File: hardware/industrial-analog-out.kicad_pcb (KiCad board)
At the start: 2 copper layers, 40 x 40 mm, 52 parts, among them P1 CON-SENSOR2, P2 CONN_8, P3 DEBUG, P4 BOOT, U1 LMR62014X, U2 XMC1XXX24, U3 DACX760, U4 DRILL, U5 DRILL, U6 DRILL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

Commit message: Add all logos
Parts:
- added G***: LOGO, kicad-libraries:Logo_CoMCU, B.Cu at (124.6, 116.3)
- VAL: footprint kicad-libraries:WEEE_7mm_back -> kicad-libraries:WEEE_7mm
- moved VAL 32.2 mm to (146.6, 116.3)
- moved VAL 18.7 mm to (135.6, 116.3), turned to 270 degrees

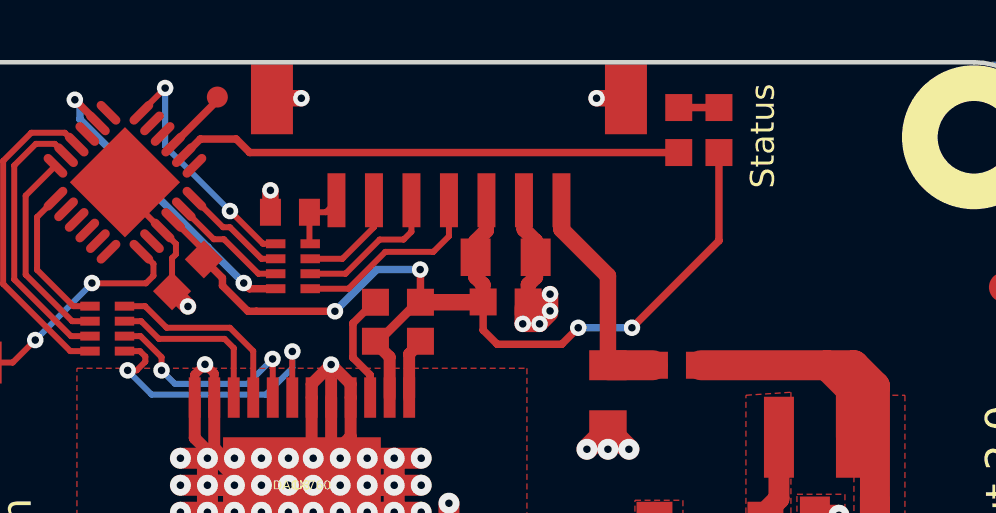
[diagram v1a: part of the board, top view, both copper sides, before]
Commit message: added second led, not fully routed
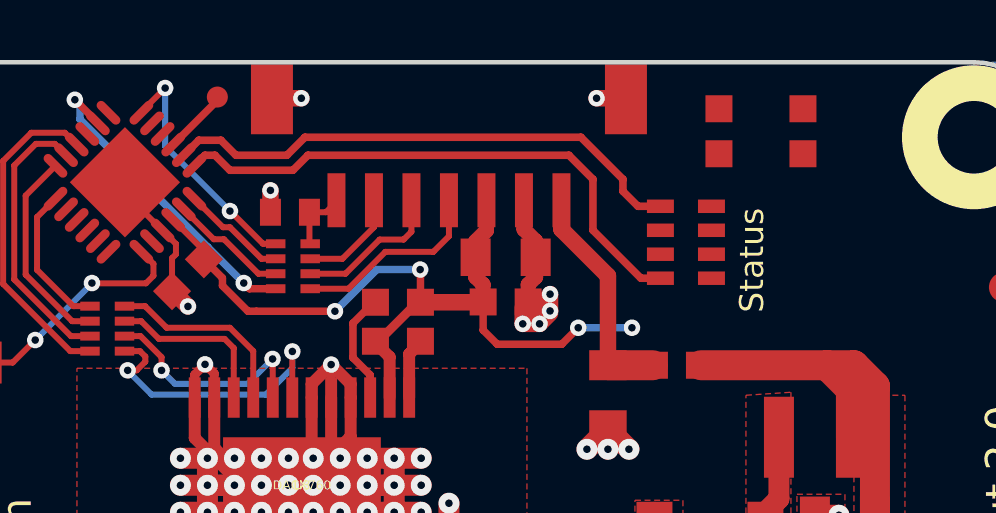
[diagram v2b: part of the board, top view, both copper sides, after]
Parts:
- removed R9: 1k, kicad-libraries:R0603F
- added D6: LED, kicad-libraries:D0603F, F.Cu at (147.4, 82.3)
- added RP3: 1k, kicad-libraries:4X0603, F.Cu at (143.5, 86.0)
- turned D5 to 270 degrees
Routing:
- net Net-(RP3-Pad5): track 0.00 -> 18.8 mm
- net 3V3: track 35.0 -> 28.0 mm
- net Net-(D5-Pad2): track 1.34 -> 0.00 mm
- net Net-(RP3-Pad8): track 16.9 -> 17.7 mm

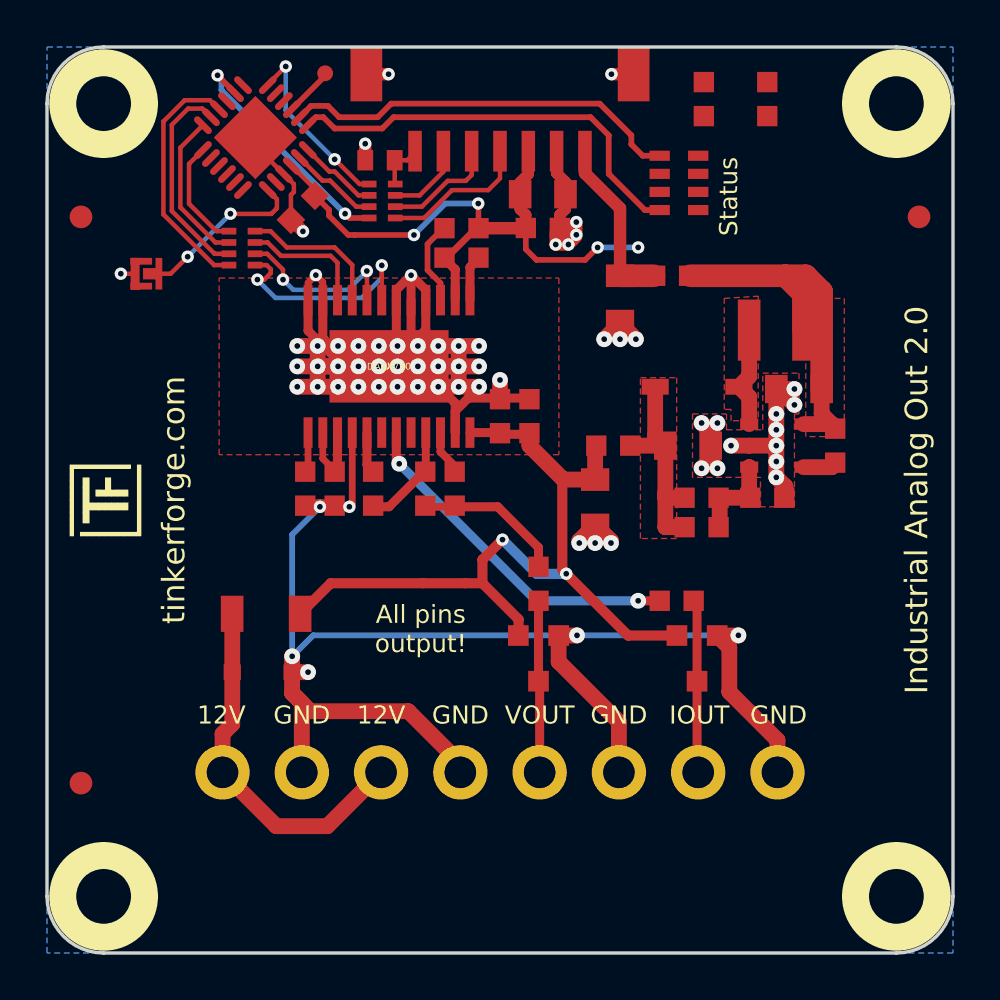
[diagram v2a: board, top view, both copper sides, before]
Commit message: routing finished, logo placement fixed
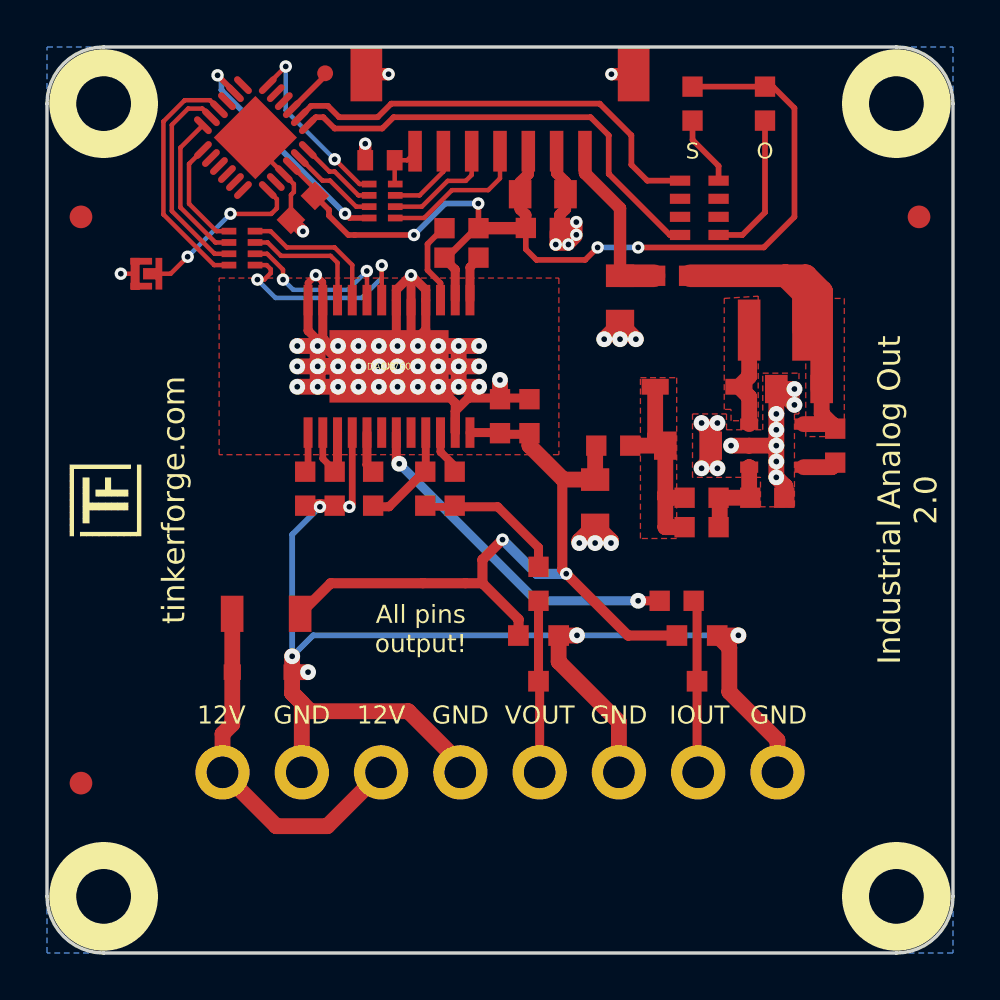
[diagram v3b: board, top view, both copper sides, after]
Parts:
- moved G*** 26.6 mm to (145.6, 100.0), turned to 90 degrees
- moved VAL 26.6 mm to (125.6, 100.0), turned to 90 degrees
- moved VAL 16.3 mm to (135.6, 100.0), turned to 90 degrees
- moved RP3 1.42 mm to (144.4, 87.1)
- moved D5 0.54 mm to (144.1, 82.5)
- moved D6 0.22 mm to (147.3, 82.5)
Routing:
- net 3V3: track 28.0 -> 45.2 mm
- net Net-(D6-Pad2): track 0.00 -> 6.51 mm
- net Net-(D5-Pad2): track 0.00 -> 3.13 mm
- net Net-(RP3-Pad8): track 17.7 -> 19.6 mm
- net Net-(RP3-Pad5): track 18.8 -> 20.1 mm
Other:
- board text added: "O"
- board text added: "S"
- board text removed: "Status"
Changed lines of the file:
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@@
-(kicad_pcb (version 4) (host pcbnew 4.0.7-e2-6376~58~ubuntu16.04.1)
+(kicad_pcb (version 4) (host pcbnew 4.0.7-e2-6376~58~ubuntu17.04.1)
   (general
     (links 115)
-    (no_connects 4)
-    (area 115.524999 79.924999 155.675001 120.075001)
+    (no_connects 0)
+    (area 13.58714 79.144999 156.455001 195.49)
     (thickness 1.6)
-    (drawings 21)
-    (tracks 522)
+    (drawings 22)
+    (tracks 534)
     (zones 0)
     (modules 54)
@@
   )
   (module kicad-libraries:D0603F (layer F.Cu)
-    (at 144.6 82.3 270)
+    (at 144.1 82.5 270)
     (attr smd)
     (fp_text reference D5 (at -0.775 0.45 270) (layer F.Fab)
@@
   )
   (module kicad-libraries:CE_5mm (layer B.Cu)
-    (at 146.6 116.3 270)
-    (fp_text reference VAL (at 0 0 270) (layer B.SilkS) hide
+    (at 125.6 100 90)
+    (fp_text reference VAL (at 0 0 90) (layer B.SilkS) hide
       (effects (font (size 0.2 0.2) (thickness 0.05)) (justify mirror))
     )
-    (fp_text value CE_5mm (at 0 0 270) (layer B.SilkS) hide
+    (fp_text value CE_5mm (at 0 0 90) (layer B.SilkS) hide
       (effects (font (size 0.2 0.2) (thickness 0.05)) (justify mirror))
     )
@@
   )
   (module kicad-libraries:WEEE_7mm (layer B.Cu)
-    (at 135.6 116.3 270)
-    (fp_text reference VAL (at 0 0 270) (layer B.SilkS) hide
+    (at 135.6 100 90)
+    (fp_text reference VAL (at 0 0 90) (layer B.SilkS) hide
       (effects (font (size 0.2 0.2) (thickness 0.05)) (justify mirror))
     )
-    (fp_text value WEEE_7mm_back (at 0.75 0 270) (layer B.SilkS) hide
+    (fp_text value WEEE_7mm_back (at 0.75 0 90) (layer B.SilkS) hide
       (effects (font (size 0.2 0.2) (thickness 0.05)) (justify mirror))
     )
@@
   )
   (module kicad-libraries:Logo_CoMCU (layer B.Cu)
-    (at 124.6 116.3 270)
-    (fp_text reference G*** (at 0 0 270) (layer B.SilkS) hide
+    (at 145.6 100 90)
+    (fp_text reference G*** (at 0 0 90) (layer B.SilkS) hide
       (effects (font (thickness 0.3)) (justify mirror))
     )
-    (fp_text value LOGO (at 0.75 0 270) (layer B.SilkS) hide
+    (fp_text value LOGO (at 0.75 0 90) (layer B.SilkS) hide
       (effects (font (thickness 0.3)) (justify mirror))
     )
@@
   )
   (module kicad-libraries:D0603F (layer F.Cu)
-    (at 147.4 82.3 270)
+    (at 147.3 82.5 270)
     (attr smd)
     (fp_text reference D6 (at -0.775 0.45 270) (layer F.Fab)
@@
   )
   (module kicad-libraries:4X0603 (layer F.Cu)
-    (at 143.5 86 270)
+    (at 144.4 87.1 270)
     (fp_text reference RP3 (at -0.61 0 270) (layer F.Fab)
       (effects (font (size 0.29972 0.29972) (thickness 0.07493)))
@@
     )
   )
-  (gr_text Status (at 145.7 86.6 90) (layer F.SilkS)
-    (effects (font (size 0.8 0.8) (thickness 0.15)))
+  (gr_text O (at 147.3 84.6) (layer F.SilkS)
+    (effects (font (size 0.7 0.7) (thickness 0.15)))
+  )
+  (gr_text S (at 144.1 84.6) (layer F.SilkS)
+    (effects (font (size 0.7 0.7) (thickness 0.15)))
   )
   (gr_text "All pins\noutput!" (at 132.1 105.7) (layer F.SilkS)
@@
     (effects (font (size 1.5 1.5) (thickness 0.3)))
   )
-  (gr_text "Industrial Analog Out 2.0" (at 154 100 90) (layer F.SilkS)
+  (gr_text "Industrial Analog Out\n2.0" (at 153.6 100 90) (layer F.SilkS)
     (effects (font (size 1 1) (thickness 0.15)))
   )
@@
   (gr_arc (start 118.1 117.5) (end 118.1 120) (angle 90) (layer Edge.Cuts) (width 0.15))
   (gr_arc (start 153.1 117.5) (end 155.6 117.5) (angle 90) (layer Edge.Cuts) (width 0.15))
-  (segment (start 136.74 88.93) (end 136.74 87.99) (width 0.25) (layer F.Cu) (net 1))
-  (segment (start 137.21 89.4) (end 136.74 88.93) (width 0.25) (layer F.Cu) (net 1))
-  (segment (start 139.36 89.4) (end 137.21 89.4) (width 0.25) (layer F.Cu) (net 1))
-  (segment (start 139.91 88.85) (end 139.36 89.4) (width 0.25) (layer F.Cu) (net 1))
-  (via (at 139.91 88.85) (size 0.55) (drill 0.25) (layers F.Cu B.Cu) (net 1))
-  (segment (start 141.7 88.85) (end 139.91 88.85) (width 0.25) (layer B.Cu) (net 1))
+  (segment (start 141.7 88.85) (end 147.25 88.85) (width 0.254) (layer F.Cu) (net 1))
   (via (at 141.7 88.85) (size 0.55) (drill 0.25) (layers F.Cu B.Cu) (net 1))
+  (segment (start 141.7 88.85) (end 139.91 88.85) (width 0.25) (layer B.Cu) (net 1))
+  (via (at 139.91 88.85) (size 0.55) (drill 0.25) (layers F.Cu B.Cu) (net 1))
+  (segment (start 139.91 88.85) (end 139.36 89.4) (width 0.25) (layer F.Cu) (net 1))
+  (segment (start 139.36 89.4) (end 137.21 89.4) (width 0.25) (layer F.Cu) (net 1))
+  (segment (start 137.21 89.4) (end 136.74 88.93) (width 0.25) (layer F.Cu) (net 1))
+  (segment (start 136.74 87.99) (end 136.74 88.93) (width 0.25) (layer F.Cu) (net 1))
+  (segment (start 148.6 82.7) (end 147.65 81.75) (width 0.254) (layer F.Cu) (net 1))
+  (segment (start 148.6 87.5) (end 148.6 82.7) (width 0.254) (layer F.Cu) (net 1))
+  (segment (start 147.25 88.85) (end 148.6 87.5) (width 0.254) (layer F.Cu) (net 1))
+  (segment (start 147.65 81.75) (end 147.3 81.75) (width 0.254) (layer F.Cu) (net 1))
+  (segment (start 144.1 81.75) (end 147.3 81.75) (width 0.254) (layer F.Cu) (net 1))
   (segment (start 127.43033 86.56967) (end 127.43033 86.57033) (width 0.25) (layer F.Cu) (net 1))
   (segment (start 127.43033 86.57033) (end 128.05 87.19) (width 0.25) (layer F.Cu) (net 1))
@@
   (segment (start 131.5 85) (end 131.85 84.65) (width 0.2) (layer F.Cu) (net 26))
   (segment (start 131.85 84.65) (end 131.85 84.6) (width 0.2) (layer F.Cu) (net 26))
+  (segment (start 145.2509 85.90112) (end 145.2509 85.2509) (width 0.254) (layer F.Cu) (net 27))
+  (segment (start 144.1 84.1) (end 144.1 83.25) (width 0.254) (layer F.Cu) (net 27))
+  (segment (start 145.2509 85.2509) (end 144.1 84.1) (width 0.254) (layer F.Cu) (net 27))
   (segment (start 127.88 81.16) (end 127.88 81.273553) (width 0.25) (layer F.Cu) (net 28))
   (segment (start 127.88 81.273553) (end 126.408668 82.744885) (width 0.25) (layer F.Cu) (net 28))
@@
   (segment (start 120.74 87.39) (end 120.74 83.29) (width 0.2) (layer F.Cu) (net 41))
   (segment (start 122.9793 89.6293) (end 120.74 87.39) (width 0.2) (layer F.Cu) (net 41))
-  (segment (start 142.6491 87.19888) (end 141.99888 87.19888) (width 0.254) (layer F.Cu) (net 55))
-  (segment (start 127.8 83.1) (end 127.467767 83.1) (width 0.254) (layer F.Cu) (net 55))
-  (segment (start 128.3 83.6) (end 127.8 83.1) (width 0.254) (layer F.Cu) (net 55))
-  (segment (start 130.4 83.6) (end 128.3 83.6) (width 0.254) (layer F.Cu) (net 55))
-  (segment (start 130.9 83.1) (end 130.4 83.6) (width 0.254) (layer F.Cu) (net 55))
-  (segment (start 139.6 83.1) (end 130.9 83.1) (width 0.254) (layer F.Cu) (net 55))
-  (segment (start 140.4 83.9) (end 139.6 83.1) (width 0.254) (layer F.Cu) (net 55))
+  (segment (start 145.2509 88.29888) (end 146.30112 88.29888) (width 0.254) (layer F.Cu) (net 52))
+  (segment (start 147.3 87.3) (end 147.3 83.25) (width 0.254) (layer F.Cu) (net 52))
+  (segment (start 146.30112 88.29888) (end 147.3 87.3) (width 0.254) (layer F.Cu) (net 52))
+  (segment (start 140.4 85.6) (end 143.09888 88.29888) (width 0.254) (layer F.Cu) (net 55))
   (segment (start 140.4 85.6) (end 140.4 83.9) (width 0.254) (layer F.Cu) (net 55))
-  (segment (start 141.99888 87.19888) (end 140.4 85.6) (width 0.254) (layer F.Cu) (net 55))
+  (segment (start 140.4 83.9) (end 139.6 83.1) (width 0.254) (layer F.Cu) (net 55))
+  (segment (start 139.6 83.1) (end 130.9 83.1) (width 0.254) (layer F.Cu) (net 55))
+  (segment (start 130.9 83.1) (end 130.4 83.6) (width 0.254) (layer F.Cu) (net 55))
+  (segment (start 130.4 83.6) (end 128.3 83.6) (width 0.254) (layer F.Cu) (net 55))
+  (segment (start 128.3 83.6) (end 127.8 83.1) (width 0.254) (layer F.Cu) (net 55))
+  (segment (start 127.467767 83.1) (end 127.8 83.1) (width 0.254) (layer F.Cu) (net 55))
+  (segment (start 143.09888 88.29888) (end 143.5491 88.29888) (width 0.254) (layer F.Cu) (net 55))
   (segment (start 127.467767 83.1) (end 127.115775 83.451992) (width 0.254) (layer F.Cu) (net 55))
-  (segment (start 126.762221 83.098439) (end 127.26066 82.6) (width 0.254) (layer F.Cu) (net 58))
-  (segment (start 141.90112 84.80112) (end 142.6491 84.80112) (width 0.254) (layer F.Cu) (net 58))
-  (segment (start 141.4 84.3) (end 141.90112 84.80112) (width 0.254) (layer F.Cu) (net 58))
-  (segment (start 141.4 83.9) (end 141.4 84.3) (width 0.254) (layer F.Cu) (net 58))
-  (segment (start 140 82.5) (end 141.4 83.9) (width 0.254) (layer F.Cu) (net 58))
-  (segment (start 130.8 82.5) (end 140 82.5) (width 0.254) (layer F.Cu) (net 58))
-  (segment (start 130.2 83.1) (end 130.8 82.5) (width 0.254) (layer F.Cu) (net 58))
-  (segment (start 128.5 83.1) (end 130.2 83.1) (width 0.254) (layer F.Cu) (net 58))
-  (segment (start 128 82.6) (end 128.5 83.1) (width 0.254) (layer F.Cu) (net 58))
+  (segment (start 143.5491 85.90112) (end 142.10112 85.90112) (width 0.254) (layer F.Cu) (net 58))
   (segment (start 127.26066 82.6) (end 128 82.6) (width 0.254) (layer F.Cu) (net 58))
+  (segment (start 128 82.6) (end 128.5 83.1) (width 0.254) (layer F.Cu) (net 58))
+  (segment (start 128.5 83.1) (end 130.2 83.1) (width 0.254) (layer F.Cu) (net 58))
+  (segment (start 130.2 83.1) (end 130.8 82.5) (width 0.254) (layer F.Cu) (net 58))
+  (segment (start 130.8 82.5) (end 140 82.5) (width 0.254) (layer F.Cu) (net 58))
+  (segment (start 140 82.5) (end 141.4 83.9) (width 0.254) (layer F.Cu) (net 58))
+  (segment (start 127.26066 82.6) (end 126.762221 83.098439) (width 0.254) (layer F.Cu) (net 58))
+  (segment (start 141.4 85.2) (end 141.4 83.9) (width 0.254) (layer F.Cu) (net 58))
+  (segment (start 142.10112 85.90112) (end 141.4 85.2) (width 0.254) (layer F.Cu) (net 58))
   (segment (start 126.762221 83.098439) (end 126.771561 83.098439) (width 0.25) (layer F.Cu) (net 58))
   (zone (net 2) (net_name GND) (layer F.Cu) (hatch edge 0.508)

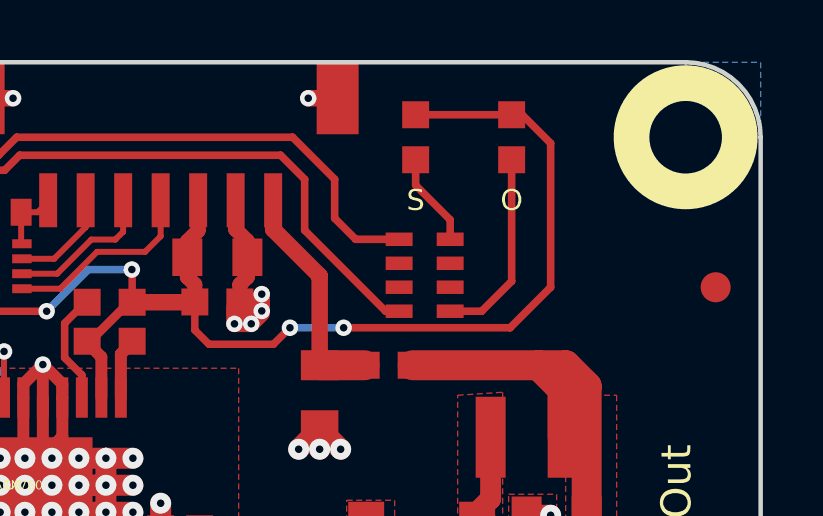
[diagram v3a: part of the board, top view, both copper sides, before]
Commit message: fix status text
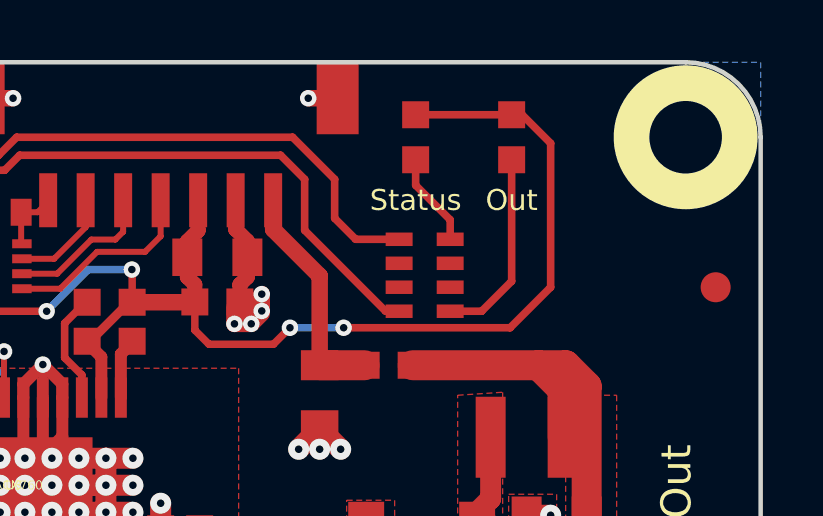
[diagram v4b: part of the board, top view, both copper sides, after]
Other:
- board text added: "Out"
- board text added: "Status"
- board text removed: "O"
- board text removed: "S"
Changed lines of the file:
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@@
   (layers
     (0 F.Cu signal)
-    (31 B.Cu signal)
+    (31 B.Cu signal hide)
     (32 B.Adhes user)
     (33 F.Adhes user)
@@
     )
   )
-  (gr_text O (at 147.3 84.6) (layer F.SilkS)
+  (gr_text Out (at 147.3 84.6) (layer F.SilkS)
     (effects (font (size 0.7 0.7) (thickness 0.15)))
   )
-  (gr_text S (at 144.1 84.6) (layer F.SilkS)
+  (gr_text Status (at 144.1 84.6) (layer F.SilkS)
     (effects (font (size 0.7 0.7) (thickness 0.15)))
   )
